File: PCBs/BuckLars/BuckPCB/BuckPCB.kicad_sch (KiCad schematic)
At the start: 64 parts, among them J1 POWER_IN, J2 Program_header, J3 5V, J4 12V, J5 Main board header, Q1 IRLIZ44N, Q2 IRLIZ44N, Q3 IRLIZ44N, Q4 IRLIZ44N, SW1 RESET, SW2 BOOT, U1 ESP32-WROOM-32D, U2 LT1936, U3 LF2304NTR, U4 LF2304NTR

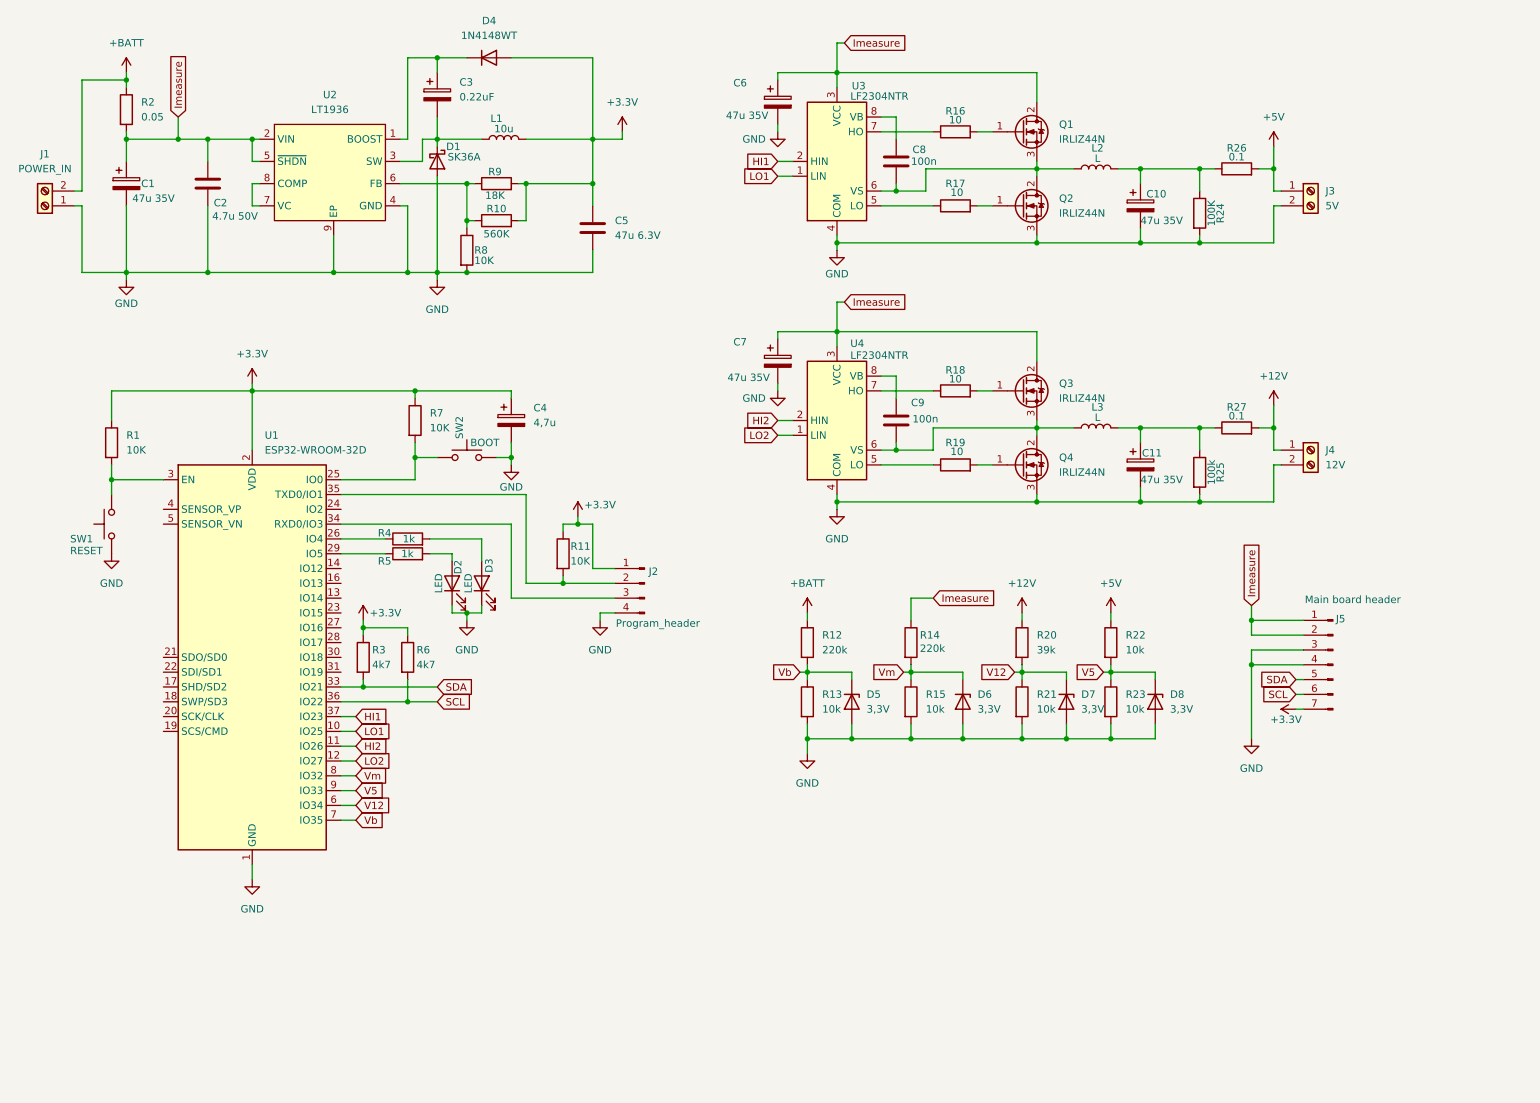
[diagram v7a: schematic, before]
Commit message: added 5V buck
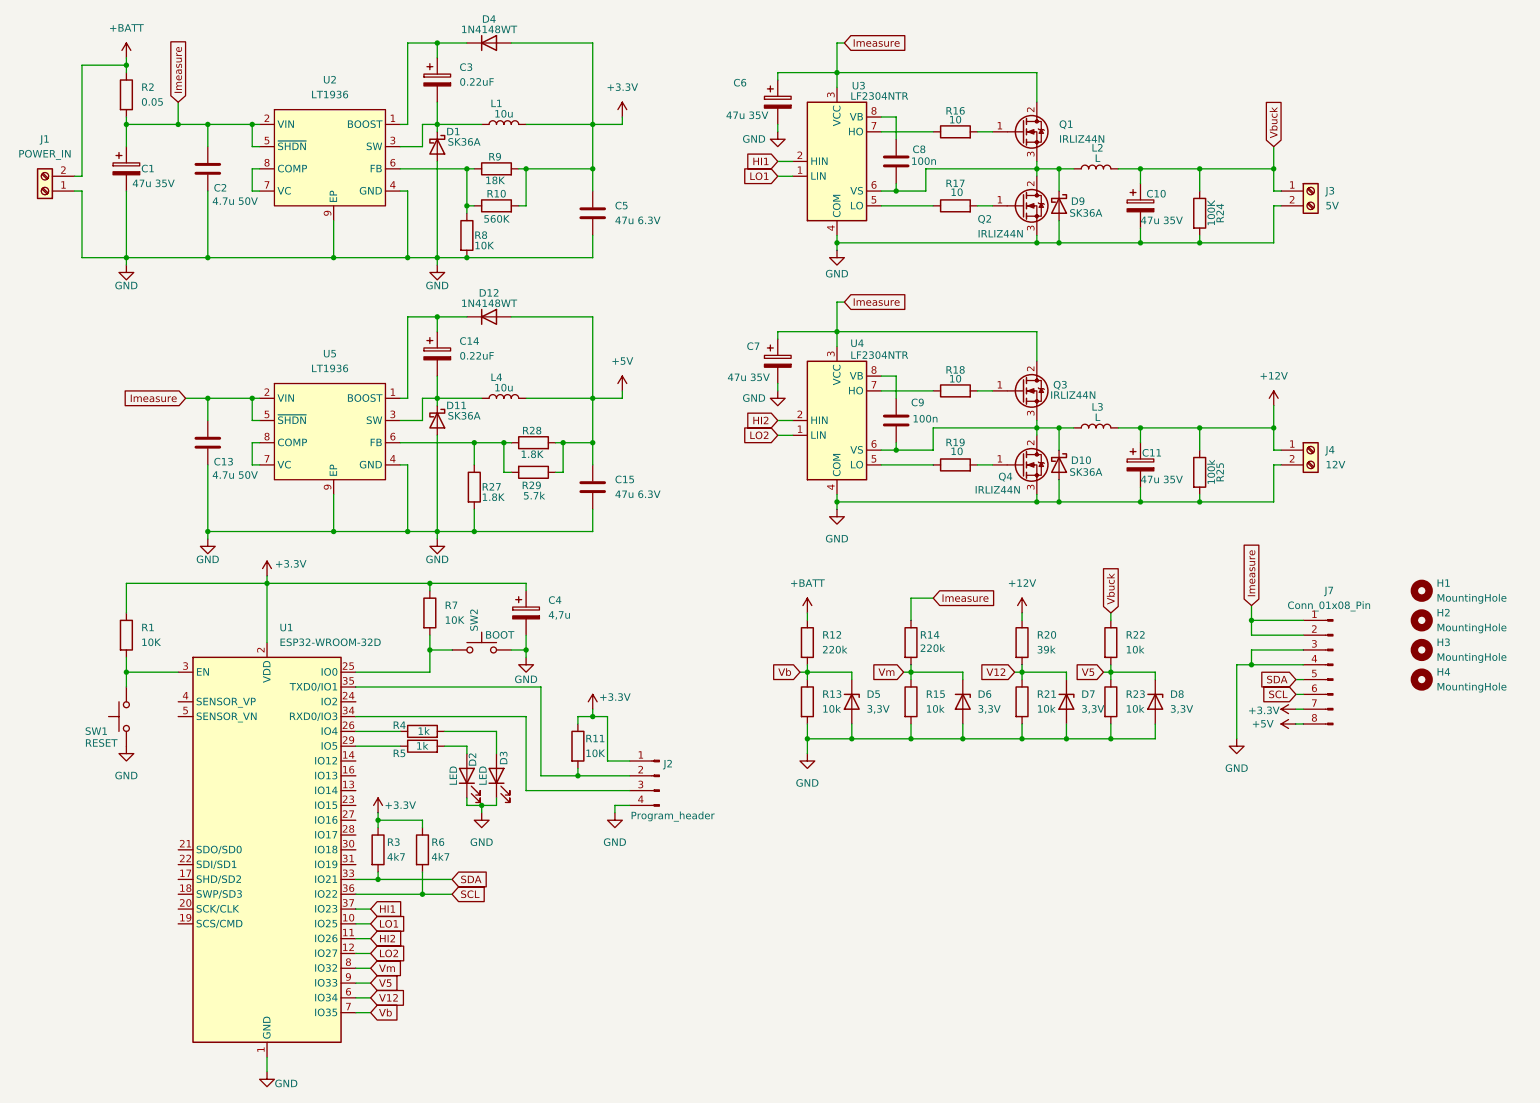
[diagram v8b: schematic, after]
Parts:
- removed J5: Main board header, Connector_PinHeader_2.54mm:PinHeader_1x07_P2.54mm_Vertical, symbol Connector:Conn_01x07_Pin
- removed R26: 0.1, Resistor_SMD:R_1206_3216Metric_Pad1.30x1.75mm_HandSolder, symbol Device:R
- added C13: 4.7u 50V, Diode_SMD:D_1206_3216Metric_Pad1.42x1.75mm_HandSolder, symbol Device:C
- added C14: 0.22uF, Capacitor_SMD:C_1206_3216Metric_Pad1.33x1.80mm_HandSolder, symbol Device:C_Polarized
- added C15: 47u 6.3V, Diode_SMD:D_1206_3216Metric_Pad1.42x1.75mm_HandSolder, symbol Device:C
- added D10, D11, D9: SK36A, Diode_SMD:D_SMC-RM10_Universal_Handsoldering, symbol Device:D_Schottky
- added D12: 1N4148WT, Diode_SMD:D_SOD-523, symbol Diode:1N4148WT
- added H1, H2, H3, H4: MountingHole, MountingHole:MountingHole_3.2mm_M3_ISO14580, symbol Mechanical:MountingHole
- added J7: Conn_01x08_Pin, Connector_PinHeader_2.54mm:PinHeader_1x08_P2.54mm_Vertical, symbol Connector:Conn_01x08_Pin
- added L4: 10u, Inductor_SMD:L_7.3x7.3_H4.5, symbol Device:L
- added R28: 1.8K, Resistor_SMD:R_1206_3216Metric_Pad1.30x1.75mm_HandSolder, symbol Device:R
- added R29: 5.7k, Resistor_SMD:R_1206_3216Metric_Pad1.30x1.75mm_HandSolder, symbol Device:R
- added U5: LT1936, Package_SO:MSOP-8-1EP_3x3mm_P0.65mm_EP1.95x2.15mm, symbol New_Library:LT1936
- R27: value 0.1 -> 1.8K
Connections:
- net +12V: now also C11.1, L3.2, R25.1; no longer R27.2
- net +3.3V: now also J7.7 (Pin_7)
- net +5V: now also C15.1, D12.2 (A), J7.8 (Pin_8), L4.2, R28.2, R29.1; no longer J3.1 (Pin_1), R22.1
- net GND: now also R27.2, C13.2, C15.2, D10.2 (A), D11.2 (A), D9.2 (A), J7.3 (Pin_3), J7.4 (Pin_4), U5.4 (GND), U5.9 (EP)
- net Imeasure: now also C13.1, J7.1 (Pin_1), J7.2 (Pin_2), U5.2 (VIN), U5.5 (~{SHDN})
- net SCL: now also J7.6 (Pin_6)
- net SDA: now also J7.5 (Pin_5)
- net at C9.2, L3.1, Q3.3 (S)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: now also D10.1 (K)
- net at C8.2, L2.1, Q1.3 (S)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: now also D9.1 (K)
- net Vbuck: now reaches C10.1, L2.2, R24.1
- net Vbuck: now also J3.1 (Pin_1), R22.1
- new net: C14.2, D11.1 (K), L4.1, U5.3 (SW)
- new net: C14.1, D12.1 (K), U5.1 (BOOST)
- new net: R27.1, R28.1, R29.2, U5.6 (FB)
- new net: U5.7 (VC), U5.8 (COMP)
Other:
- moved on the sheet: C1, C2, C3, C4, C5, D1, D2, D3, D4, J1, J2, L1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
